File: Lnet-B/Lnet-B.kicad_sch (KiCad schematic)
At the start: 12 parts, among them J6 RJ12, J7 RJ12, Q2 BC847, U5 LM311

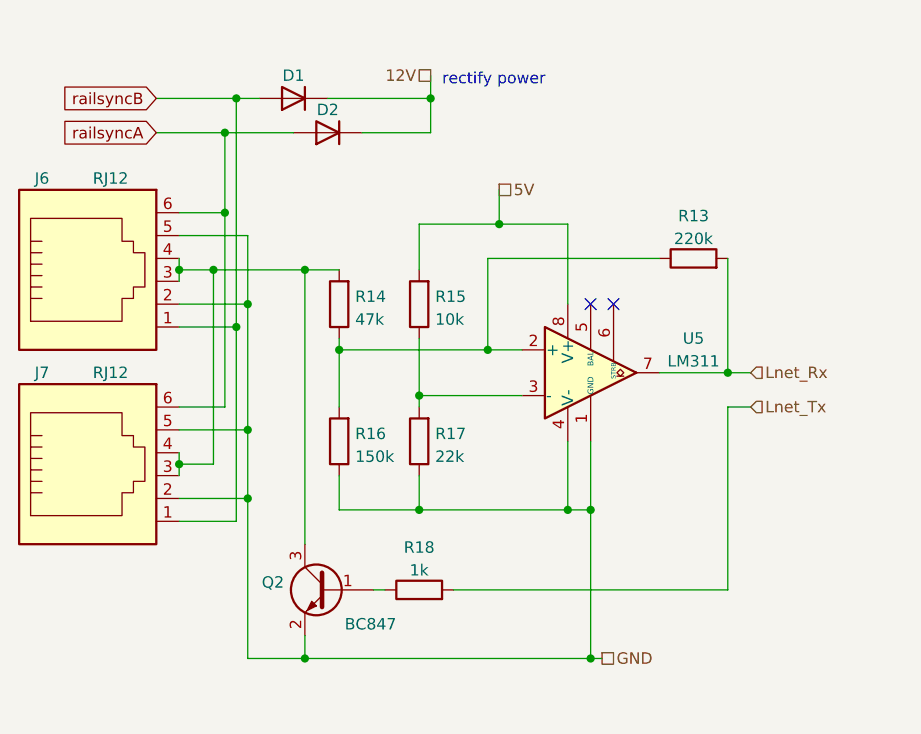
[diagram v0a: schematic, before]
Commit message: moved some schematic scheets to their own folders and routed a board with it. This allow for re-use of PCB parts.
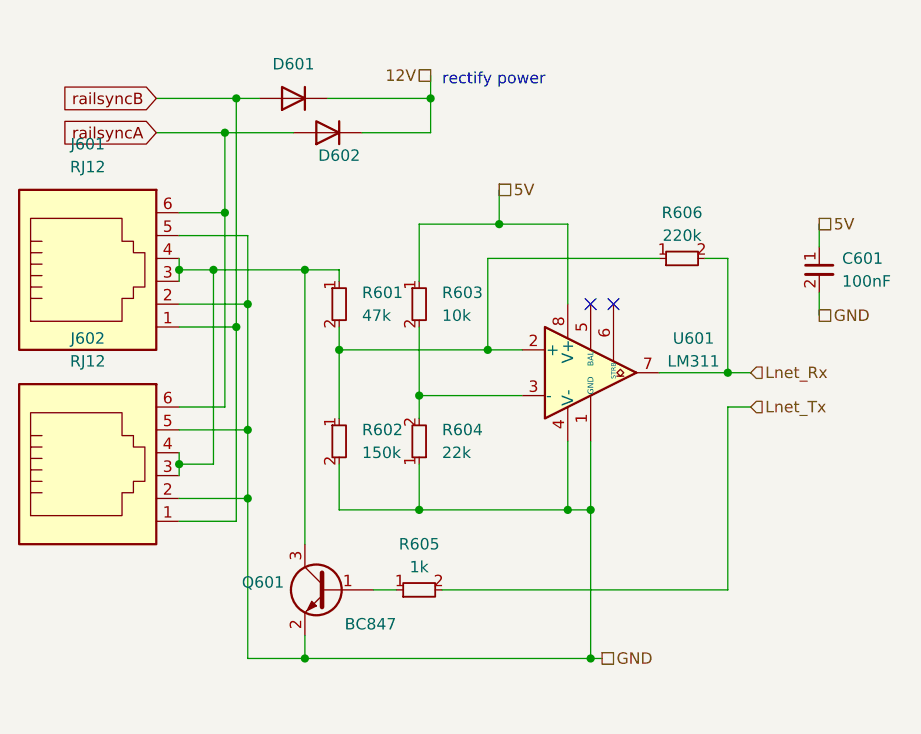
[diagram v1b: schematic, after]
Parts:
- removed D1, D2: D, Diode_SMD:D_SMA, symbol Device:D
- removed J6, J7: RJ12, Connector_RJ:RJ25_Wayconn_MJEA-660X1_Horizontal, symbol Connector:RJ12
- removed R13: 220k, Resistor_SMD:R_0805_2012Metric_Pad1.20x1.40mm_HandSolder, symbol Device:R
- removed R14: 47k, Resistor_SMD:R_0805_2012Metric_Pad1.20x1.40mm_HandSolder, symbol Device:R
- removed R15: 10k, Resistor_SMD:R_0805_2012Metric_Pad1.20x1.40mm_HandSolder, symbol Device:R
- removed R16: 150k, Resistor_SMD:R_0805_2012Metric_Pad1.20x1.40mm_HandSolder, symbol Device:R
- removed R17: 22k, Resistor_SMD:R_0805_2012Metric_Pad1.20x1.40mm_HandSolder, symbol Device:R
- removed R18: 1k, Resistor_SMD:R_0603_1608Metric_Pad0.98x0.95mm_HandSolder, symbol Device:R
- added C601: 100nF, Capacitor_SMD:C_0402_1005Metric, symbol capacitor_miscellaneous:C_0402_100nF
- added D601, D602: SM4007, Diode_SMD:D_SOD-123F, symbol Diode:SM4007
- added J601, J602: RJ12, custom_kicad_lib_sk:RJ12, symbol custom_kicad_lib_sk:RJ12
- added R601: 47k, custom_kicad_lib_sk:R_0603_smalltext, symbol resistors_0603:R_47k_0603
- added R602: 150k, custom_kicad_lib_sk:R_0603_smalltext, symbol resistors_0603:R_150k_0603
- added R603: 10k, custom_kicad_lib_sk:R_0603_smalltext, symbol resistors_0603:R_10k_0603
- added R604: 22k, custom_kicad_lib_sk:R_0603_smalltext, symbol resistors_0603:R_22k_0603
- added R605: 1k, custom_kicad_lib_sk:R_0603_smalltext, symbol resistors_0603:R_1k_0603
- added R606: 220k, custom_kicad_lib_sk:R_0603_smalltext, symbol resistors_0603:R_220k_0603
- renumbered Q2 to Q601, U5 to U601
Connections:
- net 12V: now also D601.1 (K), D602.1 (K)
- net 5V: now also C601.1, R603.1
- net GND: now also C601.2, J601.2, J601.5, J602.2, J602.5, R602.2, R604.1
- net Lnet_Rx: now also R606.2
- net Lnet_Tx: now also R605.2
- net railsyncA: now also D602.2 (A), J601.6, J602.6
- net railsyncB: now also D601.2 (A), J601.1, J602.1
- net at Q601.1 (B): now also R605.1
- net at U601.2 (+): now also R601.2, R602.1, R606.1
- net at U601.3 (-): now also R603.2, R604.2
- net at Q601.3 (C): now also J601.3, J601.4, J602.3, J602.4, R601.1

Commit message: added 12V boost converter (300mA max!)
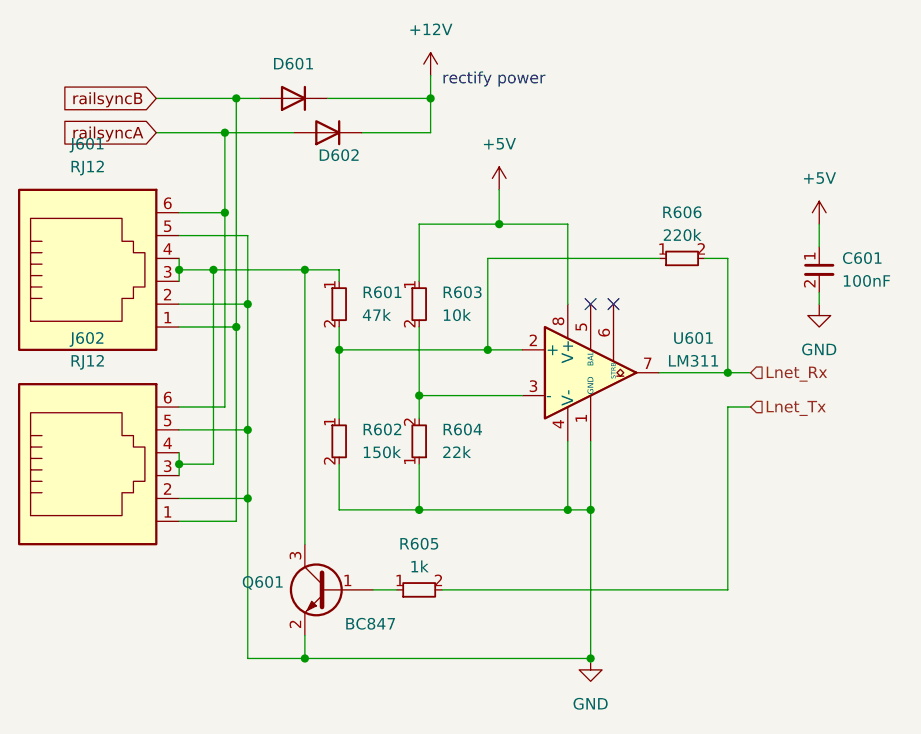
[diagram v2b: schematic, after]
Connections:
- net 12V renamed +12V
- net 5V renamed +5V
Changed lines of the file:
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@@
-    (stroke (width 0) (type default))
-  )
-  (wire (pts (xy 125.73 124.46) (xy 127 124.46))
     (stroke (width 0) (type default))
   )
@@
     (stroke (width 0) (type default))
   )
-  (wire (pts (xy 151.13 83.82) (xy 151.13 86.36))
+  (wire (pts (xy 151.13 83.82) (xy 151.13 85.09))
     (stroke (width 0) (type default))
   )
@@
     )
   )
-  (hierarchical_label "GND" (shape passive) (at 151.13 86.36 0) (fields_autoplaced)
-    (effects (font (size 1.27 1.27)) (justify left))
-  )
-  (hierarchical_label "5V" (shape passive) (at 115.57 72.39 0) (fields_autoplaced)
-    (effects (font (size 1.27 1.27)) (justify left))
-  )
   (hierarchical_label "Lnet_Tx" (shape input) (at 143.51 96.52 0) (fields_autoplaced)
     (effects (font (size 1.27 1.27)) (justify left))
   )
-  (hierarchical_label "12V" (shape passive) (at 107.95 59.69 180) (fields_autoplaced)
-    (effects (font (size 1.27 1.27)) (justify right))
-  )
-  (hierarchical_label "5V" (shape passive) (at 151.13 76.2 0) (fields_autoplaced)
-    (effects (font (size 1.27 1.27)) (justify left))
-  )
   (hierarchical_label "Lnet_Rx" (shape input) (at 143.51 92.71 0) (fields_autoplaced)
     (effects (font (size 1.27 1.27)) (justify left))
   )
-  (hierarchical_label "GND" (shape passive) (at 127 124.46 0) (fields_autoplaced)
-    (effects (font (size 1.27 1.27)) (justify left))
-  )
   (symbol (lib_id "resistors_0603:R_22k_0603") (at 106.68 100.33 180) (unit 1)
     (in_bom yes) (on_board yes) (dnp no) (fields_autoplaced)
@@
         (path "/01279bc5-94d4-4f32-b32b-510b905bfb07"
           (reference "R604") (unit 1)
+        )
+      )
+    )
+  )
+  (symbol (lib_id "power:+5V") (at 115.57 72.39 0) (unit 1)
+    (in_bom yes) (on_board yes) (dnp no) (fields_autoplaced)
+    (property "Reference" "#PWR0102" (at 115.57 76.2 0)
+      (effects (font (size 1.27 1.27)) hide)
+    )
+    (property "Value" "+5V" (at 115.57 67.31 0)
+      (effects (font (size 1.27 1.27)))
+    )
+    (property "Footprint" "" (at 115.57 72.39 0)
+      (effects (font (size 1.27 1.27)) hide)
+    )
+    (property "Datasheet" "" (at 115.57 72.39 0)
+      (effects (font (size 1.27 1.27)) hide)
+    )
+    (pin "1")
+    (instances
+      (project "Lnet-B"
+        (path "/01279bc5-94d4-4f32-b32b-510b905bfb07"
+          (reference "#PWR0102") (unit 1)
         )
       )
@@
     )
   )
+  (symbol (lib_id "power:+5V") (at 151.13 76.2 0) (unit 1)
+    (in_bom yes) (on_board yes) (dnp no) (fields_autoplaced)
+    (property "Reference" "#PWR0101" (at 151.13 80.01 0)
+      (effects (font (size 1.27 1.27)) hide)
+    )
+    (property "Value" "+5V" (at 151.13 71.12 0)
+      (effects (font (size 1.27 1.27)))
+    )
+    (property "Footprint" "" (at 151.13 76.2 0)
+      (effects (font (size 1.27 1.27)) hide)
+    )
+    (property "Datasheet" "" (at 151.13 76.2 0)
+      (effects (font (size 1.27 1.27)) hide)
+    )
+    (pin "1")
+    (instances
+      (project "Lnet-B"
+        (path "/01279bc5-94d4-4f32-b32b-510b905bfb07"
+          (reference "#PWR0101") (unit 1)
+        )
+      )
+    )
+  )
   (symbol (lib_id "Transistor_BJT:BC847") (at 96.52 116.84 0) (mirror y) (unit 1)
     (in_bom yes) (on_board yes) (dnp no)
@@
         (path "/01279bc5-94d4-4f32-b32b-510b905bfb07"
           (reference "R606") (unit 1)
+        )
+      )
+    )
+  )
+  (symbol (lib_id "power:GND") (at 151.13 85.09 0) (unit 1)
+    (in_bom yes) (on_board yes) (dnp no) (fields_autoplaced)
+    (property "Reference" "#PWR0104" (at 151.13 91.44 0)
+      (effects (font (size 1.27 1.27)) hide)
+    )
+    (property "Value" "GND" (at 151.13 90.17 0)
+      (effects (font (size 1.27 1.27)))
+    )
+    (property "Footprint" "" (at 151.13 85.09 0)
+      (effects (font (size 1.27 1.27)) hide)
+    )
+    (property "Datasheet" "" (at 151.13 85.09 0)
+      (effects (font (size 1.27 1.27)) hide)
+    )
+    (pin "1")
+    (instances
+      (project "Lnet-B"
+        (path "/01279bc5-94d4-4f32-b32b-510b905bfb07"
+          (reference "#PWR0104") (unit 1)
         )
       )
@@
     )
   )
+  (symbol (lib_id "power:+12V") (at 107.95 59.69 0) (unit 1)
+    (in_bom yes) (on_board yes) (dnp no) (fields_autoplaced)
+    (property "Reference" "#PWR0103" (at 107.95 63.5 0)
+      (effects (font (size 1.27 1.27)) hide)
+    )
+    (property "Value" "+12V" (at 107.95 54.61 0)
+      (effects (font (size 1.27 1.27)))
+    )
+    (property "Footprint" "" (at 107.95 59.69 0)
+      (effects (font (size 1.27 1.27)) hide)
+    )
+    (property "Datasheet" "" (at 107.95 59.69 0)
+      (effects (font (size 1.27 1.27)) hide)
+    )
+    (pin "1")
+    (instances
+      (project "Lnet-B"
+        (path "/01279bc5-94d4-4f32-b32b-510b905bfb07"
+          (reference "#PWR0103") (unit 1)
+        )
+      )
+    )
+  )
   (symbol (lib_id "resistors_0603:R_47k_0603") (at 97.79 85.09 0) (unit 1)
     (in_bom yes) (on_board yes) (dnp no) (fields_autoplaced)
@@
         )
       )
+    )
+  )
+  (symbol (lib_id "power:GND") (at 125.73 124.46 0) (unit 1)
+    (in_bom yes) (on_board yes) (dnp no) (fields_autoplaced)
+    (property "Reference" "#PWR0105" (at 125.73 130.81 0)
+      (effects (font (size 1.27 1.27)) hide)
+    )
+    (property "Value" "GND" (at 125.73 129.54 0)
+      (effects (font (size 1.27 1.27)))
+    )
+    (property "Footprint" "" (at 125.73 124.46 0)
+      (effects (font (size 1.27 1.27)) hide)
+    )
+    (property "Datasheet" "" (at 125.73 124.46 0)
+      (effects (font (size 1.27 1.27)) hide)
+    )
+    (pin "1")
+    (instances
+      (project "Lnet-B"
+        (path "/01279bc5-94d4-4f32-b32b-510b905bfb07"
+          (reference "#PWR0105") (unit 1)
+        )
+      )
